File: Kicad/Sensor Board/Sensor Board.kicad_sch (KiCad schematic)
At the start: 12 parts, among them J1 SPI, J15 TE 3-2363962-0 Connector, J2 7 pin FPC 0.3mm Panasonic Y3b, J3 free pins, J5 7 pin FPC 0.3mm Panasonic Y3b, J7 JST SH

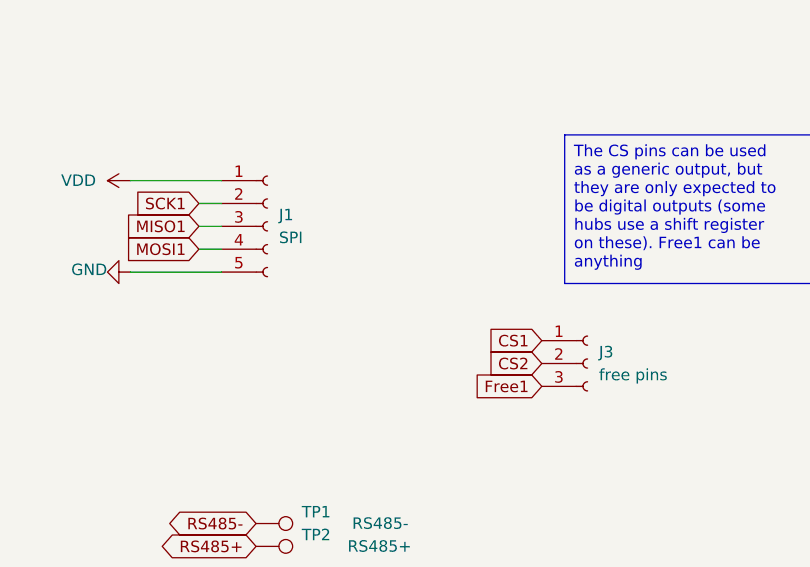
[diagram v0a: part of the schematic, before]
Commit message: Finished Sensor board and 3d models
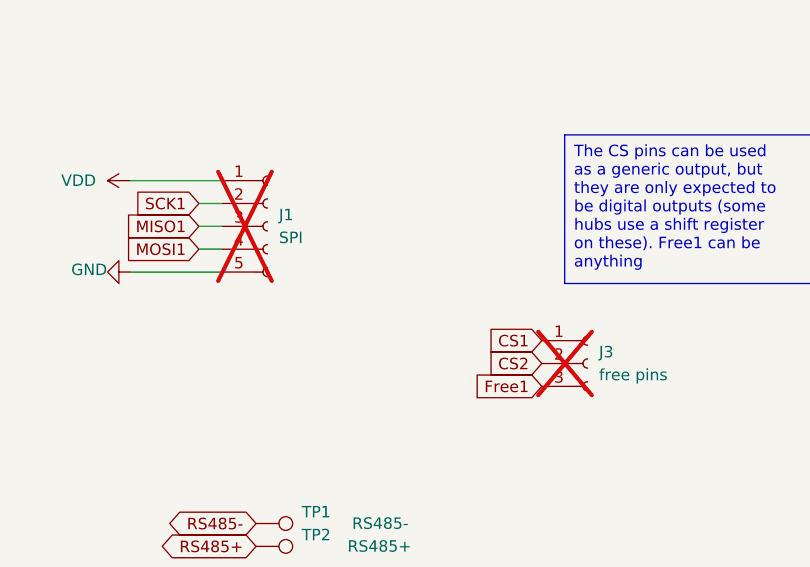
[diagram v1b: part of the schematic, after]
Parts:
- J1, J3: now not fitted
- TP1, TP2: now left out of the parts list
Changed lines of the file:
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@@
 		(unit 1)
 		(exclude_from_sim no)
-		(in_bom yes)
+		(in_bom no)
 		(on_board yes)
 		(dnp no)
@@
 		(in_bom yes)
 		(on_board yes)
-		(dnp no)
+		(dnp yes)
 		(fields_autoplaced yes)
 		(property "Reference" "J3"
@@
 		(in_bom yes)
 		(on_board yes)
-		(dnp no)
+		(dnp yes)
 		(fields_autoplaced yes)
 		(property "Reference" "J1"
@@
 		(unit 1)
 		(exclude_from_sim no)
-		(in_bom yes)
-		(on_board yes)
-		(dnp no)
+		(in_bom no)
+		(on_board yes)
+		(dnp no)

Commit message: Added LCSC part numbers, DNP attr, and exported Gerbers
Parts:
- J15: LCSC (none) -> C425104
- R2, R4: LCSC (none) -> C25804
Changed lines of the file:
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@@
+			)
+		)
+		(property "LCSC" "C25804"
+			(at 71.374 61.214 0)
+			(effects
+				(font
+					(size 1.27 1.27)
+				)
+				(hide yes)
 			)
 		)
@@
 			)
 		)
+		(property "LCSC" "C425104"
+			(at 195.326 93.472 0)
+			(effects
+				(font
+					(size 1.27 1.27)
+				)
+				(hide yes)
+			)
+		)
 		(pin "28"
 		)
@@
 			(effects
 				(font
+					(size 1.27 1.27)
+				)
+				(hide yes)
+			)
+		)
+		(property "LCSC" "C25804"
+			(at 70.104 28.194 0)
+			(effects
+				(font
